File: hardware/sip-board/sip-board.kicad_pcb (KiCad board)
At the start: 8 copper layers, 17 x 50 mm, 92 parts, among them IC1 MT25QL512ABB1EW9-0SIT, IC2 XC7S15-1CPGA196C, J1 Conn_02x03_Odd_Even, J2 Conn_01x10_Pin, J3 Conn_01x10_Pin, J4 Conn_01x10_Pin, J5 Conn_01x10_Pin, U1 TLV75718PDRV, U2 TLV75733PDRV, U3 TLV75710PDRV

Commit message: text
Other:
- board text added: "why are you looking down here?"
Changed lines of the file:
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@@
 		(layer "Edge.Cuts")
+	)
+	(gr_text "why are you looking down here?"
+		(at 116.0018 99.4918 0)
+		(layer "B.SilkS")
+		(effects
+			(font
+				(size 0.5 0.5)
+				(thickness 0.1)
+				(bold yes)
+			)
+			(justify left bottom mirror)
+		)
 	)
 	(gr_text "DQ3\n"
@@
 	)
 	(gr_text "Connor L/PSC\nUT Austin IH01\nZ80 SiP Drop-In\nSp '25"
-		(at 109.0422 53.6194 0)
+		(at 151.511 44.8564 0)
 		(layer "F.SilkS" knockout)
 		(effects

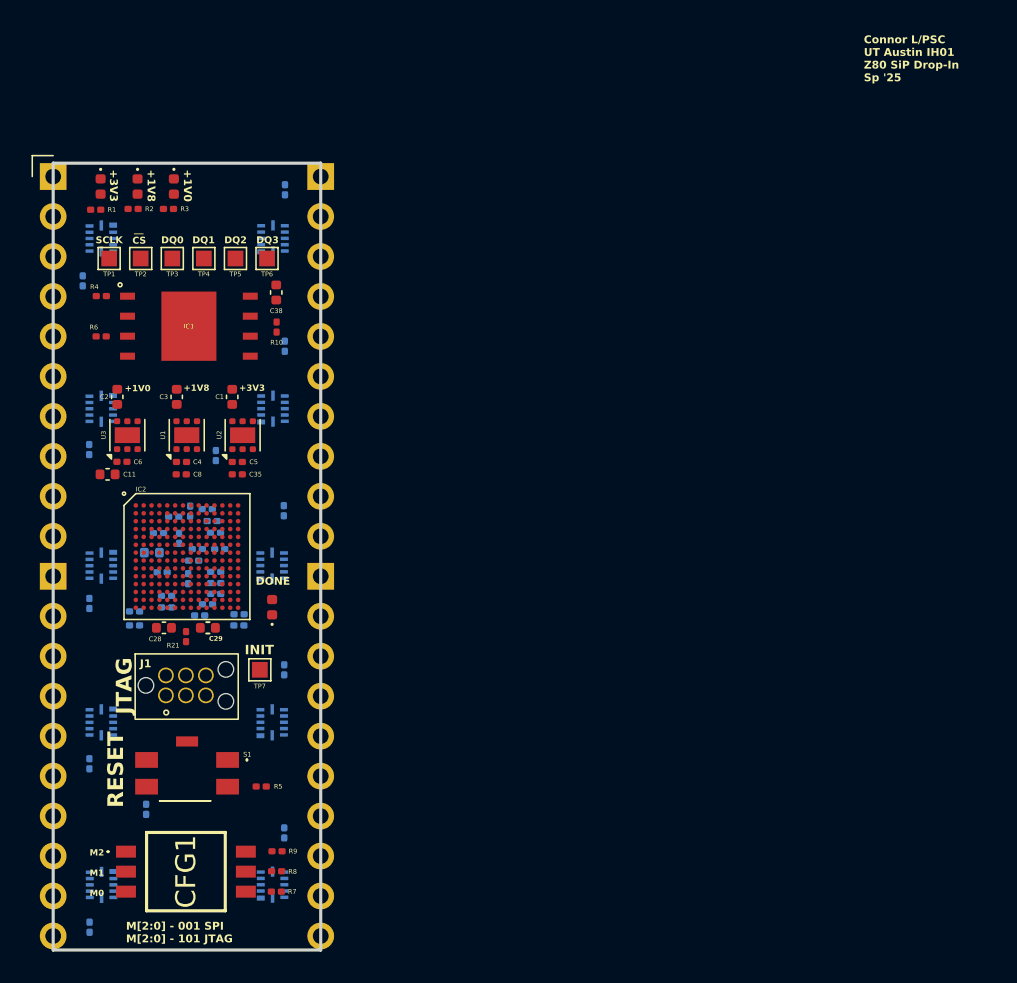
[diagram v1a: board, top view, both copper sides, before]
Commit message: stop routing need to change schematic (again)
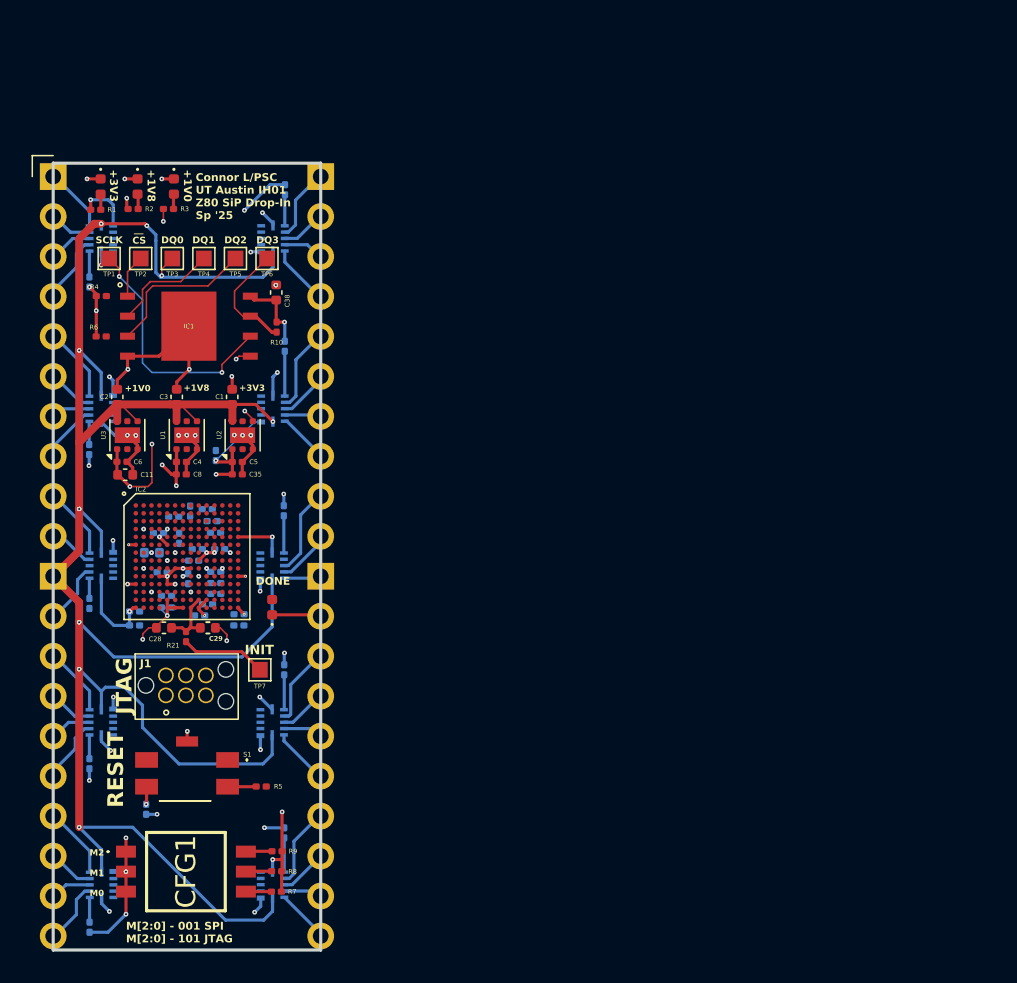
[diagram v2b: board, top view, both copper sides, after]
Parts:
- moved C11 1.12 mm to (104.6, 69.8), turned to 0 degrees
- moved R15 0.43 mm to (102.3, 57.5)
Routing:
- net +5V: track 0.00 -> 137.7 mm, vias 0 -> 8
- net GND: track 0.00 -> 70.8 mm, vias 0 -> 54
- net +3V3: track 0.00 -> 46.6 mm, vias 0 -> 22
- net +1V8: track 0.00 -> 30.3 mm, vias 0 -> 4
- net +1V0: track 0.00 -> 21.9 mm, vias 0 -> 3
- net SPI_SCK_CCLK: track 0.00 -> 15.9 mm, vias 0 -> 2
- net SPI_DQ2: track 0.00 -> 9.84 mm
- net SPI_DQ0: track 0.00 -> 9.60 mm, vias 0 -> 2
- net SPI_DQ3: track 0.00 -> 7.31 mm
- net SPI_DQ1: track 0.00 -> 6.81 mm
- net A2_5V: track 0.00 -> 5.49 mm
- net INIT_B: track 0.00 -> 5.43 mm
- net A6_5V: track 0.00 -> 5.28 mm
- net WAIT_5V: track 0.00 -> 5.06 mm
- net RFSH_5V: track 0.00 -> 4.91 mm
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- added copper zone on In1.Cu, net +1V0
- added copper zone on In3.Cu, net +1V8
- added copper zone on In4.Cu, net +3V3
- added copper zone on In1.Cu, net GND
- added copper zone on In6.Cu, net GND

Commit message: raahhhhh my eyeballs hurt
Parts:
- removed U1: TLV75718PDRV, Package_SON:WSON-6-1EP_2x2mm_P0.65mm_EP1x1.6mm
- removed U2: TLV75733PDRV, Package_SON:WSON-6-1EP_2x2mm_P0.65mm_EP1x1.6mm
- removed U3: TLV75710PDRV, Package_SON:WSON-6-1EP_2x2mm_P0.65mm_EP1x1.6mm
- added C39: 10u, Capacitor_SMD:C_0201_0603Metric, B.Cu at (109.4, 70.2)
- added IC3: LTC3569EUDC#TRPBF, hardware:QFN50P300X400X80-21N-D, F.Cu at (108.5, 67.0)
- added L1: 3u3, Capacitor_SMD:C_0201_0603Metric, B.Cu at (108.9, 64.5)
- added L2: 1u5, Capacitor_SMD:C_0201_0603Metric, B.Cu at (111.7, 66.4)
- added L3: 2u2, Capacitor_SMD:C_0201_0603Metric, B.Cu at (109.4, 69.5)
- added Q1: MBT3904DW1, Package_TO_SOT_SMD:SOT-363_SC-70-6, F.Cu at (112.3, 66.6)
- added Q2: MBT3904DW1, Package_TO_SOT_SMD:SOT-363_SC-70-6, F.Cu at (112.5, 69.5)
- added Q3: BS170F, Package_TO_SOT_SMD:SOT-23, F.Cu at (112.7, 58.1)
- added Q4: BS170F, Package_TO_SOT_SMD:SOT-23, F.Cu at (109.0, 58.1)
- added Q5: BS170F, Package_TO_SOT_SMD:SOT-23, F.Cu at (105.3, 58.1)
- added R22: 100k, Resistor_SMD:R_0201_0603Metric, F.Cu at (63.7, 61.1)
- added R23: 3.48k, 1%, Resistor_SMD:R_0201_0603Metric, F.Cu at (107.4, 69.5)
- added R24: 10k, 1%, Resistor_SMD:R_0201_0603Metric, F.Cu at (107.4, 70.2)
- added R25: 1k, Resistor_SMD:R_0201_0603Metric, B.Cu at (112.0, 65.0)
- added R26: 100k, Resistor_SMD:R_0201_0603Metric, F.Cu at (109.2, 69.8)
- added R27: 100k, Resistor_SMD:R_0201_0603Metric, F.Cu at (114.3, 69.1)
- added R28: 30k, Resistor_SMD:R_0201_0603Metric, B.Cu at (109.0, 66.1)
- added R29: 120k, 1%, Resistor_SMD:R_0201_0603Metric, F.Cu at (105.2, 66.8)
- added R30: 150k, Resistor_SMD:R_0201_0603Metric, B.Cu at (107.2, 65.2)
- added R31: 120k, 1%, Resistor_SMD:R_0201_0603Metric, F.Cu at (105.2, 66.2)
- added R32: 180k, Resistor_SMD:R_0201_0603Metric, B.Cu at (105.8, 68.7)
- added R33: 57.6k, 1%, Resistor_SMD:R_0201_0603Metric, F.Cu at (105.2, 67.4)
- added R34: UNKNOWN, Resistor_SMD:R_0201_0603Metric, F.Cu at (109.0, 60.6)
- added R35: 100k, Resistor_SMD:R_0201_0603Metric, B.Cu at (105.3, 57.5)
- added R36: UNKNOWN, Resistor_SMD:R_0201_0603Metric, F.Cu at (106.0, 60.6)
- added TP10: TestPoint, TestPoint:TestPoint_Pad_1.0x1.0mm, F.Cu at (111.8, 64.2)
- added TP11: TestPoint, TestPoint:TestPoint_Pad_1.0x1.0mm, F.Cu at (115.2, 76.2)
- added TP8: TestPoint, TestPoint:TestPoint_Pad_1.0x1.0mm, F.Cu at (106.0, 64.2)
- added TP9: TestPoint, TestPoint:TestPoint_Pad_1.0x1.0mm, F.Cu at (109.0, 64.2)
- C1: value 10u -> 22u; footprint Capacitor_SMD:C_0402_1005Metric -> Capacitor_SMD:C_0201_0603Metric
- C2: value 10u -> 20p; footprint Capacitor_SMD:C_0402_1005Metric -> Capacitor_SMD:C_0201_0603Metric; moved to B.Cu
- C3: value 10u -> 22u; footprint Capacitor_SMD:C_0402_1005Metric -> Capacitor_SMD:C_0201_0603Metric; moved to B.Cu
- C30, C31, C32, C34, C36, C37, R11, R12, R13, R14, R15, R16, R17, R18, R19, R20, U10, U11, U12, U13, U4, U5, U6, U7, U8, U9: moved to F.Cu
- C35, C8: moved to B.Cu
- C4, C6: value 100u -> 20p; moved to B.Cu
- C5: value 100u -> 10u; moved to B.Cu
- R1, R3: value R_Small -> 100k; moved to B.Cu
- R2: value R_Small -> UNKNOWN
- moved R7 84.2 mm to (32.7, 74.8)
- moved R10 83.8 mm to (32.7, 80.0), turned to 0 degrees
- moved R8 83.5 mm to (32.7, 76.5)
- moved R9 82.9 mm to (32.7, 78.3)
- moved R5 82.6 mm to (32.7, 71.3), turned to 0 degrees
- moved U13 71.4 mm to (56.2, 53.9)
- moved R6 71.3 mm to (32.7, 73.0)
- moved R4 71.2 mm to (32.7, 69.5)
- moved U7 68.3 mm to (52.3, 50.2), turned to 0 degrees
- moved U12 67.7 mm to (56.2, 50.2)
- moved R20 67.4 mm to (53.8, 63.6), turned to 0 degrees
- moved U5 66.3 mm to (52.3, 42.9), turned to 0 degrees
- moved U11 64.6 mm to (56.2, 46.5)
- moved R19 64.2 mm to (53.8, 61.9), turned to 0 degrees
- moved R14 62.8 mm to (51.3, 61.9), turned to 0 degrees
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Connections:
- C2 pad 1: +5V -> +1V0
- C2 pad 2: GND -> /Voltage Regulators - 3V3, 1V8, 1V0/FB1
- C3 pad 1: +5V -> +1V0
- C4 pad 2: GND -> /Voltage Regulators - 3V3, 1V8, 1V0/FB2
- C5 pad 1: +3V3 -> +1V8
- C6 pad 1: +1V0 -> +3V3
- C6 pad 2: GND -> /Voltage Regulators - 3V3, 1V8, 1V0/FB3
- D1 pad 1: GND -> Net-(D1-K)
- D1 pad 2: Net-(D1-A) -> +1V0
- D2 pad 1: GND -> Net-(D2-K)
- D2 pad 2: Net-(D2-A) -> +1V8
- D3 pad 1: GND -> Net-(D3-K)
- D3 pad 2: Net-(D3-A) -> +3V3
- R1 pad 1: +3V3 -> +1V0
- R1 pad 2: Net-(D1-A) -> PGOOD
- R2 pad 1: +1V8 -> Net-(D1-K)
- R2 pad 2: Net-(D2-A) -> Net-(Q3-D)
- R3 pad 1: +1V0 -> +1V8
- R3 pad 2: Net-(D3-A) -> PGOOD
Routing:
- net +5V: track 137.7 -> 0.00 mm, vias 8 -> 0
- net GND: track 70.8 -> 0.00 mm, vias 54 -> 0
- net +3V3: track 46.6 -> 0.00 mm, vias 22 -> 0
- net +1V8: track 30.3 -> 0.00 mm, vias 4 -> 0
- net +1V0: track 21.9 -> 0.00 mm, vias 3 -> 0
- net SPI_SCK_CCLK: track 15.9 -> 0.00 mm, vias 2 -> 0
- net SPI_DQ2: track 9.84 -> 0.00 mm
- net SPI_DQ0: track 9.60 -> 0.00 mm, vias 2 -> 0
- net SPI_DQ3: track 7.31 -> 0.00 mm
- net SPI_DQ1: track 6.81 -> 0.00 mm
- net A2_5V: track 5.49 -> 0.00 mm
- net INIT_B: track 5.43 -> 0.00 mm
- net A6_5V: track 5.28 -> 0.00 mm
- net WAIT_5V: track 5.06 -> 0.00 mm
- net RFSH_5V: track 4.91 -> 0.00 mm
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- removed copper zone on In1.Cu, net +1V0
- removed copper zone on In3.Cu, net +1V8
- removed copper zone on In4.Cu, net +3V3
- removed copper zone on In1.Cu, net GND
- removed copper zone on In6.Cu, net GND
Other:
- board text added: "1V0"
- board text added: "1V8"
- board text added: "3V3"
- board text added: "DQ0 SCK DQ3"
- board text added: "DQ2 DQ1 __ CS"
- board text added: "GND"
- board text added: "M[2:0]=001 QSPI M[2:0]=101 JTAG"
- board text removed: "+1V0"
- board text removed: "+1V8"
- board text removed: "+3V3"
- board text removed: "Board is 17mm wide x 50mm tall and top left is at (100, 50) Connectors holes 1.7mm diameter/width, 2.54mm pitch. Then, placement is: (100, 50 + 1.7/2) - Pins 1-10 (100, 50 + (10*2.54) + (1.7/2)) - Pins 11-20 (117, 50 + 1.7/2) - Pins 21-30 (117, 50 + (10*2.54) + (1.7/2)) - Pins 31-40"
- board text removed: "CS"
- board text removed: "Connor L/PSC UT Austin IH01 Z80 SiP Drop-In Sp '25"
- board text removed: "DONE"
- board text removed: "DQ0"
- board text removed: "DQ1"
- board text removed: "DQ2"
- board text removed: "DQ3"
- board text removed: "M[2:0] - 001 SPI M[2:0] - 101 JTAG"
- board text removed: "SCLK"
- board text removed: "__"
- board text removed: "why are you looking down here?"

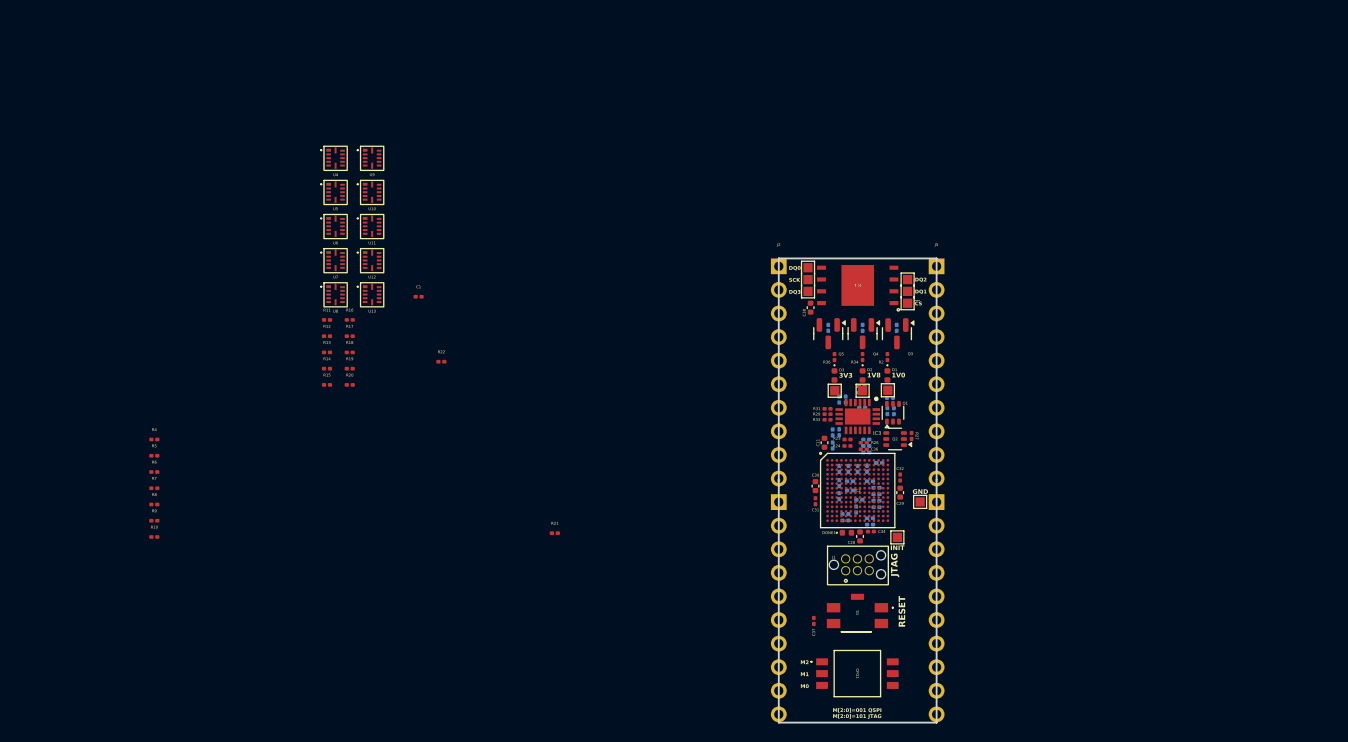
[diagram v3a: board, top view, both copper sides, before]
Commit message: non-gpio routing done for "v3" (really like v6)
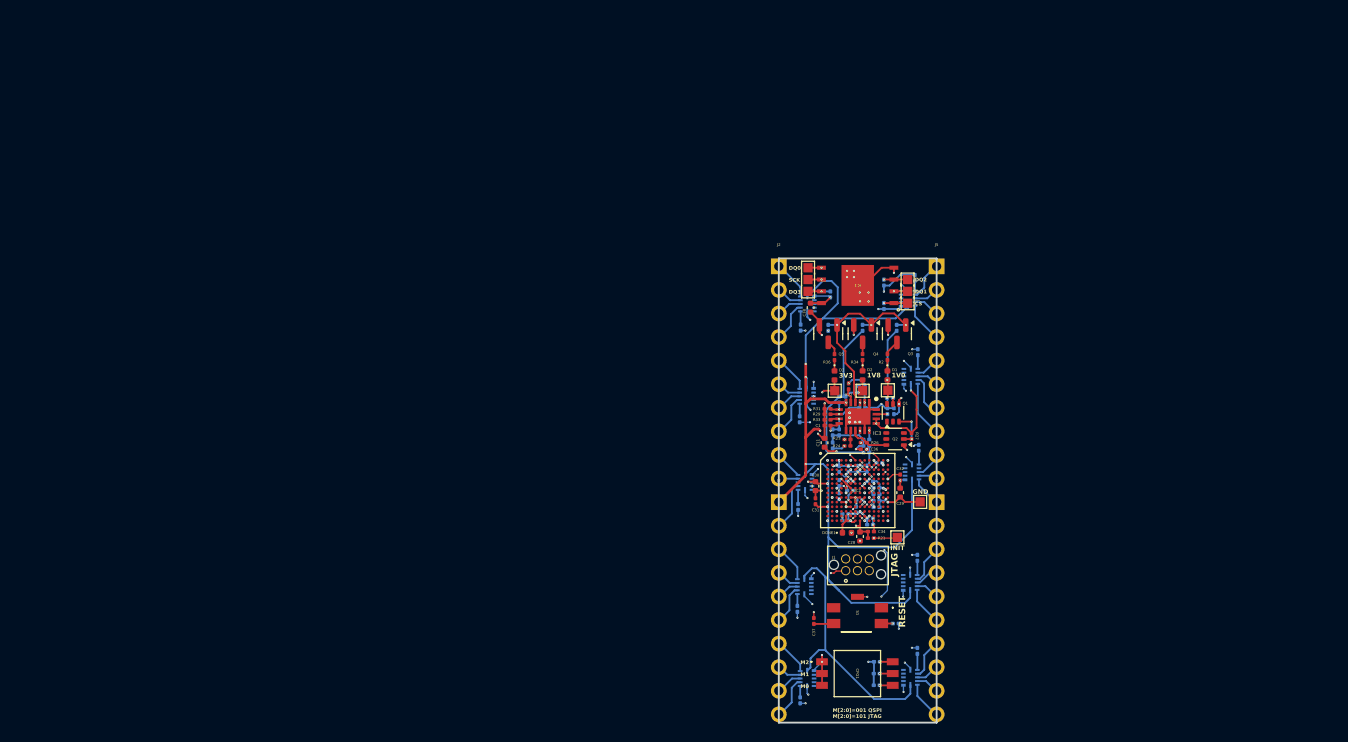
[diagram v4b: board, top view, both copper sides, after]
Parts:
- R10, R11, R12, R13, R14, R15, R16, R17, R18, R19, R20, R4, R5, R6, R7, R8, R9, U10, U11, U12, U13, U4, U5, U6, U7, U8, U9: moved to B.Cu
- moved R5 81.9 mm to (112.6, 89.3), turned to 180 degrees
- moved R6 81.2 mm to (111.3, 52.6), turned to 90 degrees
- moved R7 80.7 mm to (110.5, 96.0), turned to 180 degrees
- moved R8 79.9 mm to (110.5, 94.7), turned to 180 degrees
- moved R4 79.9 mm to (111.3, 55.1), turned to 90 degrees
- moved R9 79.3 mm to (110.6, 93.5), turned to 180 degrees
- moved R10 77.4 mm to (105.5, 53.9), turned to 90 degrees
- moved U13 71.1 mm to (114.2, 95.1)
- moved U7 67.9 mm to (103.0, 95.2), turned to 180 degrees
- moved U12 67.5 mm to (114.2, 84.9)
- moved R20 67.5 mm to (114.9, 92.3), turned to -90 degrees
- moved U5 66.0 mm to (102.8, 85.3), turned to 180 degrees
- moved R19 64.4 mm to (114.9, 82.2), turned to -90 degrees
- moved U11 63.9 mm to (114.3, 73.0)
- moved R14 62.2 mm to (102.3, 97.6), turned to 90 degrees
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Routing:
- net +5V: track 0.00 -> 141.0 mm, vias 0 -> 11
- net GND: track 0.00 -> 87.0 mm, vias 0 -> 99
- net +3V3: track 0.00 -> 56.5 mm, vias 0 -> 36
- net +1V8: track 0.00 -> 30.8 mm, vias 0 -> 6
- net SPI_DQ0: track 0.00 -> 25.3 mm, vias 0 -> 2
- net M0_CONFIG: track 0.00 -> 24.9 mm, vias 0 -> 2
- net M1_CONFIG: track 0.00 -> 23.2 mm, vias 0 -> 4
- net SPI_DQ3: track 0.00 -> 23.2 mm, vias 0 -> 2
- net SPI_DQ2: track 0.00 -> 23.0 mm, vias 0 -> 2
- net SPI_SCK_CCLK: track 0.00 -> 22.7 mm, vias 0 -> 2
- net +1V0: track 0.00 -> 22.5 mm, vias 0 -> 13
- net SPI_DQ1: track 0.00 -> 21.9 mm, vias 0 -> 2
- net M2_CONFIG: track 0.00 -> 21.8 mm, vias 0 -> 2
- net PGOOD: track 0.00 -> 21.5 mm, vias 0 -> 3
- net SPI_CS: track 0.00 -> 21.2 mm, vias 0 -> 2
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- added copper zone on In3.Cu, net +1V0
- added copper zone on In3.Cu, net +1V8
- added copper zone on In4.Cu, net +3V3
- added copper zone on In1.Cu, net GND
- added copper zone on In6.Cu, net GND

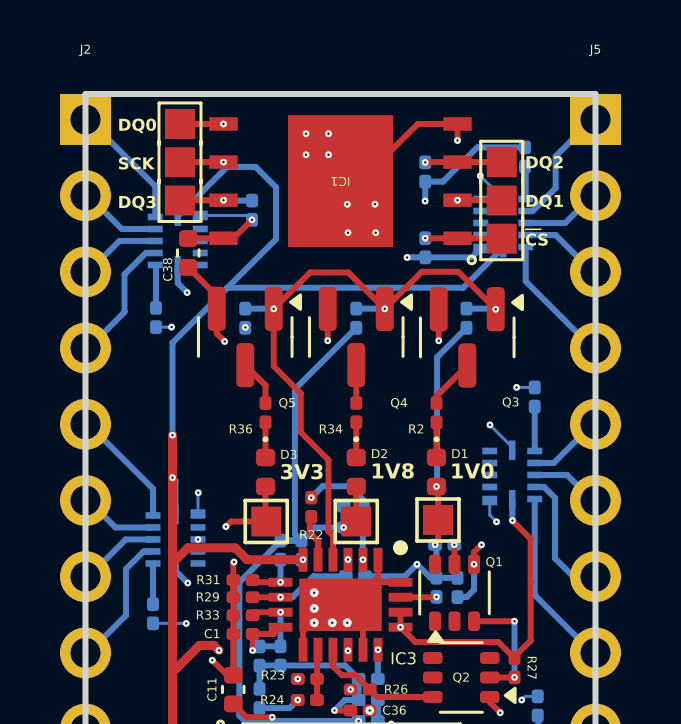
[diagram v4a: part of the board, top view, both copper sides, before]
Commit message: remove all but 3v3 LED
not enough voltage/current from the other 2 power rails to light up an LED
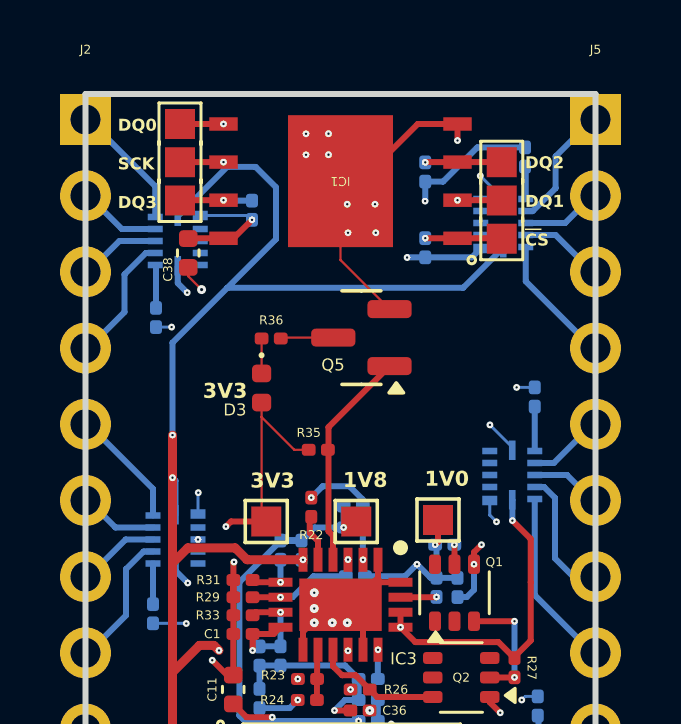
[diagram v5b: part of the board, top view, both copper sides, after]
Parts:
- removed D1, D2: LED, LED_SMD:LED_0402_1005Metric
- removed Q3, Q4: BS170F, Package_TO_SOT_SMD:SOT-23
- removed R1, R3: 100k, Resistor_SMD:R_0201_0603Metric
- removed R2, R34: UNKNOWN, Resistor_SMD:R_0201_0603Metric
- R35: moved to F.Cu
- R36: value UNKNOWN -> 100
- moved R35 5.02 mm to (107.8, 61.9), turned to 0 degrees
- moved Q5 3.87 mm to (109.2, 58.1), turned to 180 degrees
- moved D3 2.80 mm to (105.9, 59.8)
- moved R36 2.48 mm to (106.2, 58.1), turned to 0 degrees
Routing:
- net PGOOD: track 21.5 -> 7.36 mm, vias 3 -> 0
- net +1V8: track 30.8 -> 21.6 mm
- net +1V0: track 22.5 -> 15.6 mm, vias 13 -> 12
- net +3V3: track 56.5 -> 61.4 mm, vias 36 -> 35
- net Net-(Q3-D): track 1.68 -> 0.00 mm
- net Net-(Q4-D): track 1.26 -> 0.00 mm
- net Net-(D2-K): track 1.18 -> 0.00 mm
- net Net-(D1-K): track 1.17 -> 0.00 mm
- net GND: track 87.0 -> 87.8 mm, vias 99 -> 97
